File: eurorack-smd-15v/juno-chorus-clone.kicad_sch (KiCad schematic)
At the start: 162 parts, among them J1 +-15v In, P2 AUDIO_IN, P3 OUT_L, P4 OUT_R, Q1 2SC1815, Q10 2SC1815, Q11 2SA1015, Q12 2SA1015, Q13 2SC1815, Q14 2SA1015, Q15 2SA1015, Q16 2SK30, Q18 2SA1015, Q19 2SA1015, Q2 2SC1815, Q20 2SK30, Q3 2SA1015, Q4 2SA1015, Q5 2SC1815, Q6 2SC1815, Q7 2SA1015, Q8 2SA1015, Q9 2SC1815, SW1 SW_PUSH, U1 TL084HID, U11 TL084HID, U5 MN3009, U6 MN3101, U7 MN3009, U8 MN3101

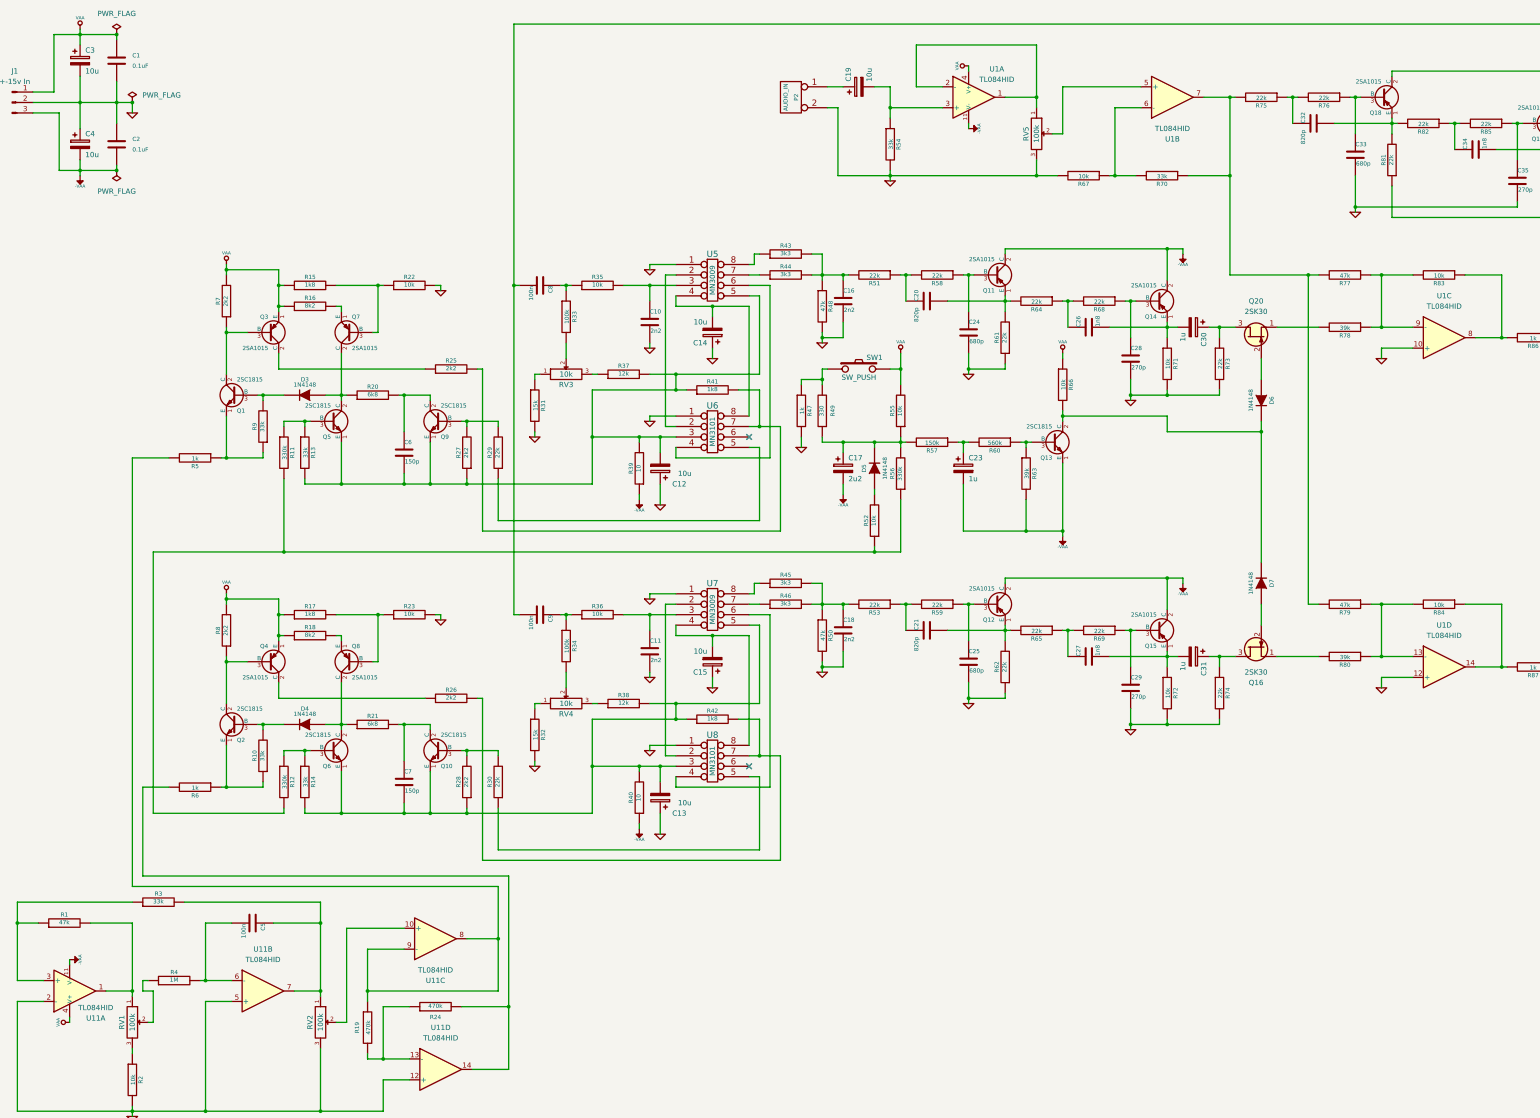
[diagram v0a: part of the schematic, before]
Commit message: Replace TL084 with TL074 to stay consistent with my other designs
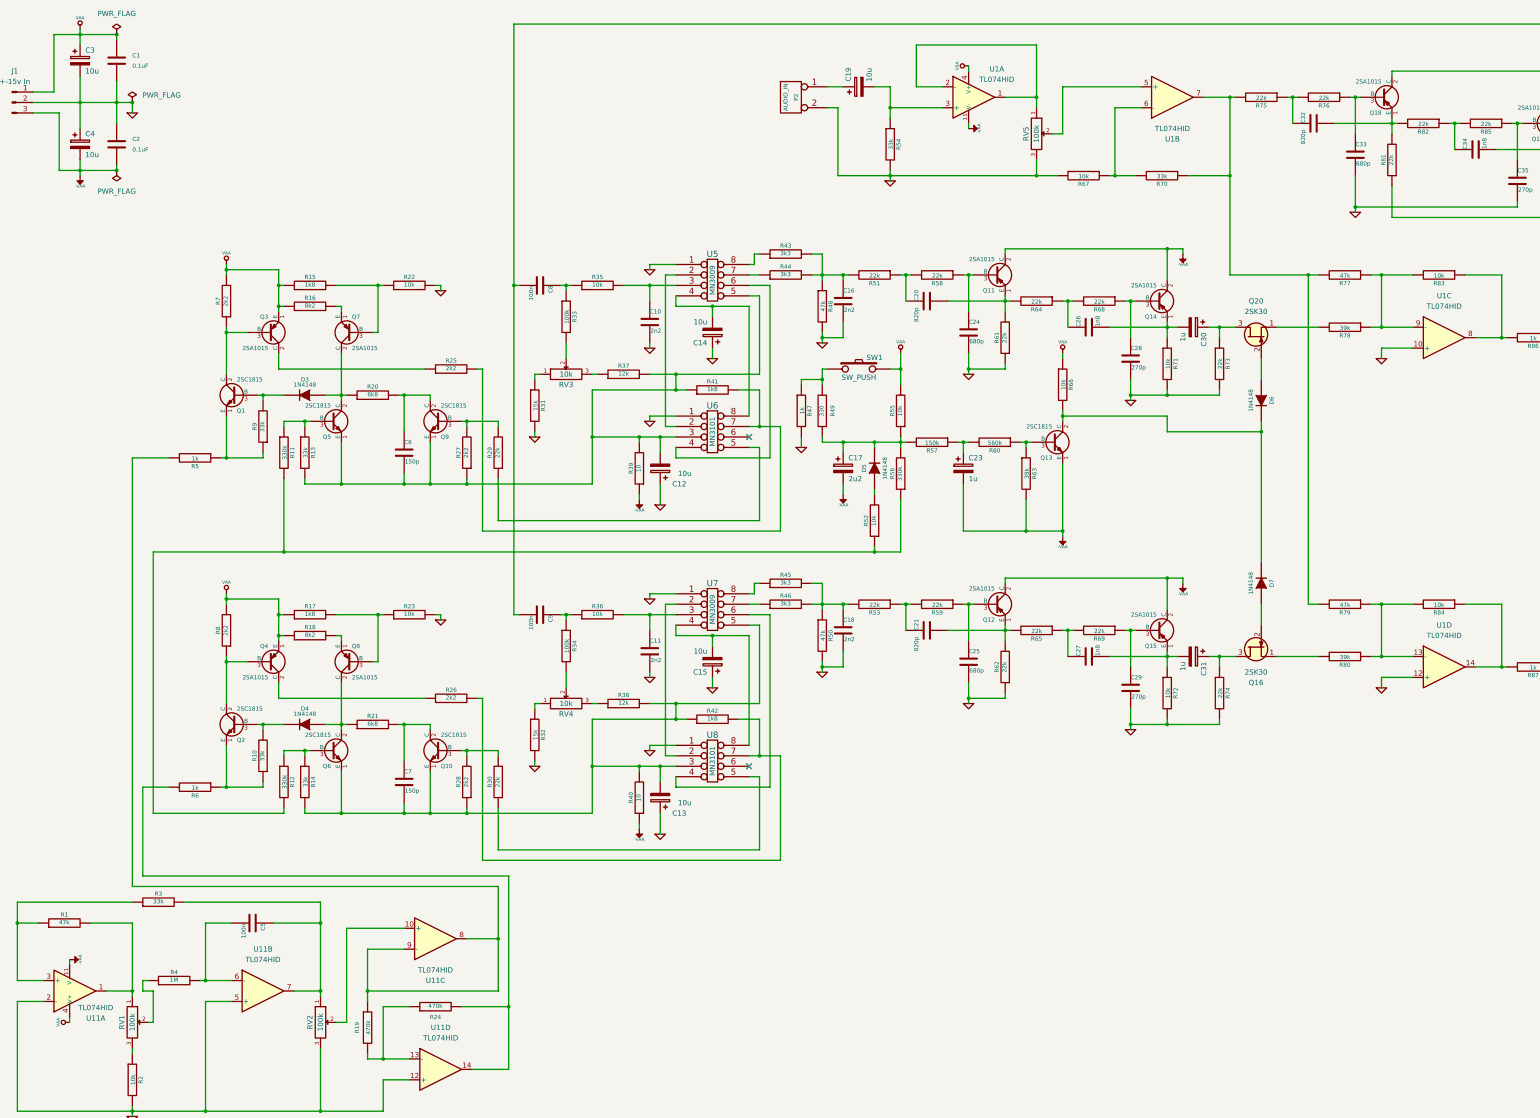
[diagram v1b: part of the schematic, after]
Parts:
- U1, U11: value TL084HID -> TL074HID
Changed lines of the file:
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@@
 			)
 		)
-		(property "Value" "TL084HID"
+		(property "Value" "TL074HID"
 			(at 255.778 31.242 0)
 			(effects
@@
 			)
 		)
-		(property "Value" "TL084HID"
+		(property "Value" "TL074HID"
 			(at 119.38 247.65 0)
 			(effects
@@
 			)
 		)
-		(property "Value" "TL084HID"
+		(property "Value" "TL074HID"
 			(at 36.83 256.794 0)
 			(effects
@@
 			)
 		)
-		(property "Value" "TL084HID"
+		(property "Value" "TL074HID"
 			(at 120.65 264.16 0)
 			(effects
@@
 			)
 		)
-		(property "Value" "TL084HID"
+		(property "Value" "TL074HID"
 			(at 364.49 86.36 0)
 			(effects
@@
 			)
 		)
-		(property "Value" "TL084HID"
+		(property "Value" "TL074HID"
 			(at 298.45 43.18 0)
 			(effects
@@
 			)
 		)
-		(property "Value" "TL084HID"
+		(property "Value" "TL074HID"
 			(at 364.49 166.37 0)
 			(effects
@@
 			)
 		)
-		(property "Value" "TL084HID"
+		(property "Value" "TL074HID"
 			(at 77.47 245.11 0)
 			(effects
